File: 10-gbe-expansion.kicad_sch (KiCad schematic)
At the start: 4 parts

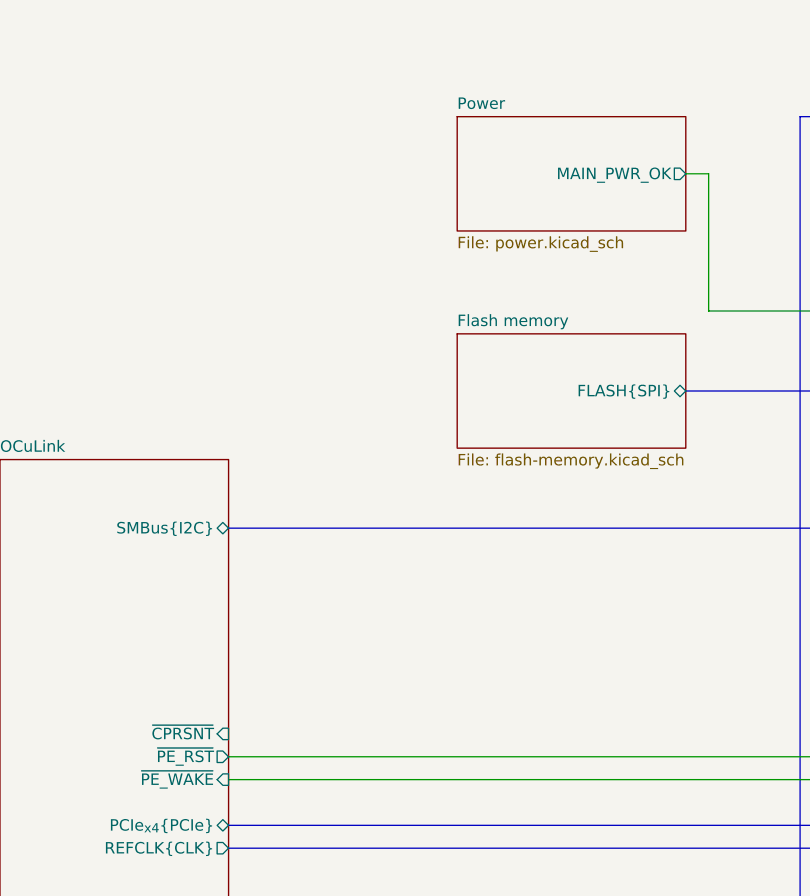
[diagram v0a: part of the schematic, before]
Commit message: [#85196] WIP: Add power sequencing, connect CPRSNT signal
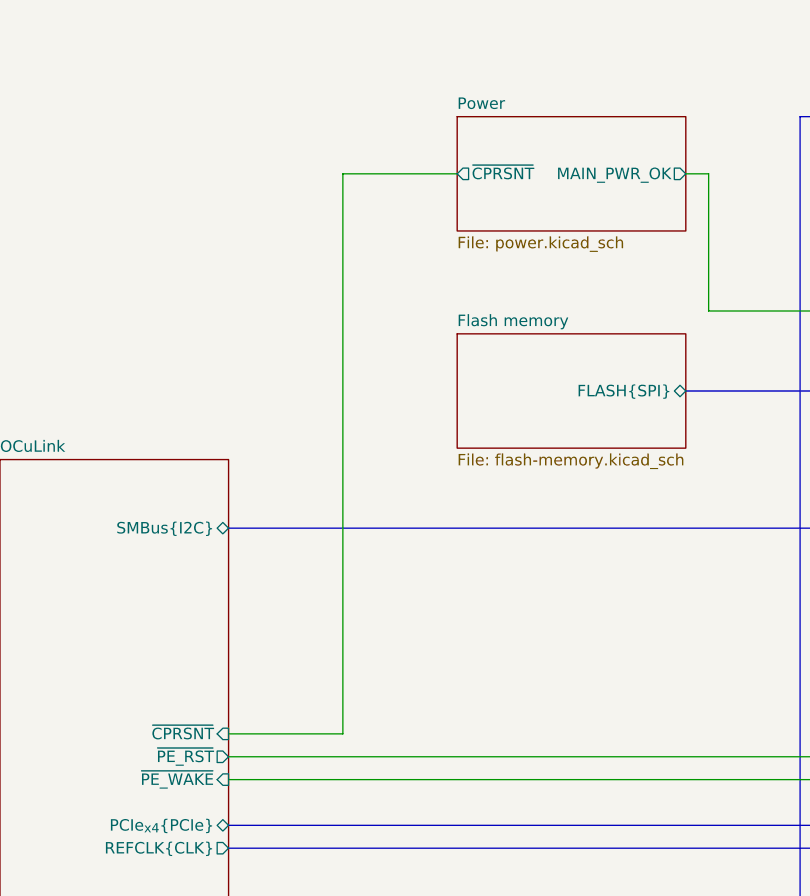
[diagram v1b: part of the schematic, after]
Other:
- sheet Power ports: added ~{CPRSNT}; removed none
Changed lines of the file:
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@@
+		)
+	)
+	(wire
+		(pts
+			(xy 88.9 95.25) (xy 88.9 157.48)
+		)
+		(stroke
+			(width 0)
+			(type default)
 		)
 	)
@@
 	(wire
 		(pts
+			(xy 88.9 157.48) (xy 76.2 157.48)
+		)
+		(stroke
+			(width 0)
+			(type default)
+		)
+	)
+	(wire
+		(pts
 			(xy 203.2 66.04) (xy 213.36 66.04)
 		)
@@
 		(pts
 			(xy 279.4 121.92) (xy 304.8 121.92)
+		)
+		(stroke
+			(width 0)
+			(type default)
+		)
+	)
+	(wire
+		(pts
+			(xy 101.6 95.25) (xy 88.9 95.25)
 		)
 		(stroke
@@
 			)
 		)
+		(pin "~{CPRSNT}" output
+			(at 101.6 95.25 180)
+			(effects
+				(font
+					(size 1.27 1.27)
+				)
+				(justify left)
+			)
+		)

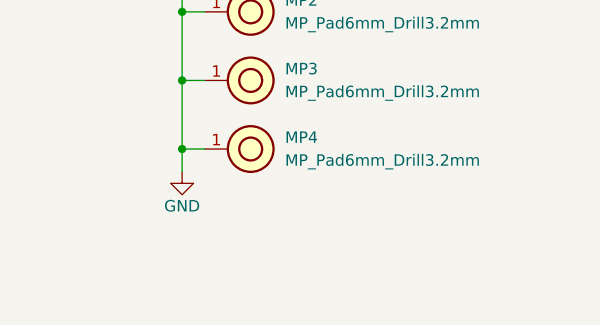
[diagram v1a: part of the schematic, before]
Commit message: [#85196] Update PCB from schematic, remove second heat sink
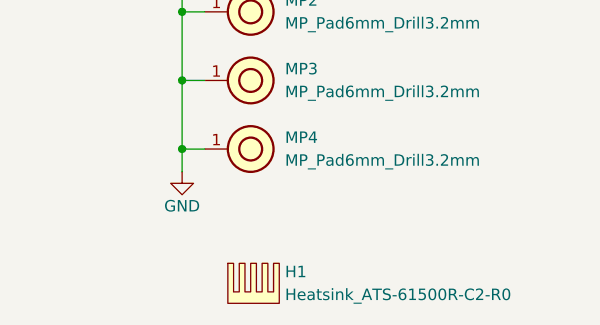
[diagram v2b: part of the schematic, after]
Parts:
- added H1: Heatsink_ATS-61500R-C2-R0, antmicro-footprints:Heatsink_ATS-61500R-C2-R0, symbol antmicroMechanicalParts:Heatsink_ATS-61500R-C2-R0
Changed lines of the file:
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@@
+	)
+	(symbol
+		(lib_id "antmicroMechanicalParts:Heatsink_ATS-61500R-C2-R0")
+		(at 328.93 217.17 0)
+		(unit 1)
+		(exclude_from_sim no)
+		(in_bom yes)
+		(on_board yes)
+		(dnp no)
+		(fields_autoplaced yes)
+		(property "Reference" "H1"
+			(at 335.28 218.1225 0)
+			(effects
+				(font
+					(size 1.27 1.27)
+					(thickness 0.15)
+				)
+				(justify left)
+			)
+		)
+		(property "Value" "Heatsink_ATS-61500R-C2-R0"
+			(at 335.28 220.6625 0)
+			(effects
+				(font
+					(size 1.27 1.27)
+					(thickness 0.15)
+				)
+				(justify left)
+			)
+		)
+		(property "Footprint" "antmicro-footprints:Heatsink_ATS-61500R-C2-R0"
+			(at 346.71 224.79 0)
+			(effects
+				(font
+					(size 1.27 1.27)
+					(thickness 0.15)
+				)
+				(justify left bottom)
+				(hide yes)
+			)
+		)
+		(property "Datasheet" "https://www.qats.com/DataSheet/ATS-61500-Series-C2-R0"
+			(at 346.71 227.33 0)
+			(effects
+				(font
+					(size 1.27 1.27)
+					(thickness 0.15)
+				)
+				(justify left bottom)
+				(hide yes)
+			)
+		)
+		(property "Description" "Heat Sinks fanSINK Assembly with Mounting Hardware"
+			(at 328.93 217.17 0)
+			(effects
+				(font
+					(size 1.27 1.27)
+				)
+				(hide yes)
+			)
+		)
+		(property "MPN" "ATS-61500R-C2-R0"
+			(at 346.71 229.87 0)
+			(effects
+				(font
+					(size 1.27 1.27)
+					(thickness 0.15)
+				)
+				(justify left bottom)
+				(hide yes)
+			)
+		)
+		(property "Manufacturer" "Advanced Thermal Solutions"
+			(at 346.71 232.41 0)
+			(effects
+				(font
+					(size 1.27 1.27)
+					(thickness 0.15)
+				)
+				(justify left bottom)
+				(hide yes)
+			)
+		)
+		(property "Author" "Antmicro"
+			(at 346.71 234.95 0)
+			(effects
+				(font
+					(size 1.27 1.27)
+					(thickness 0.15)
+				)
+				(justify left bottom)
+				(hide yes)
+			)
+		)
+		(property "License" "Apache-2.0"
+			(at 346.71 237.49 0)
+			(effects
+				(font
+					(size 1.27 1.27)
+					(thickness 0.15)
+				)
+				(justify left bottom)
+				(hide yes)
+			)
+		)
+		(instances
+			(project "10-gbe-expansion"
+				(path "/04bda987-e5eb-48b4-9e90-d8211dc11b39"
+					(reference "H1")
+					(unit 1)
+				)
+			)
+		)
 	)
 	(symbol
